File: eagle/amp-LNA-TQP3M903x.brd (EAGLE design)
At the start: 30 x 20 mm, 20 parts, among them J1 142-0701-851, J2 142-0701-851, U1 TQP3M903X

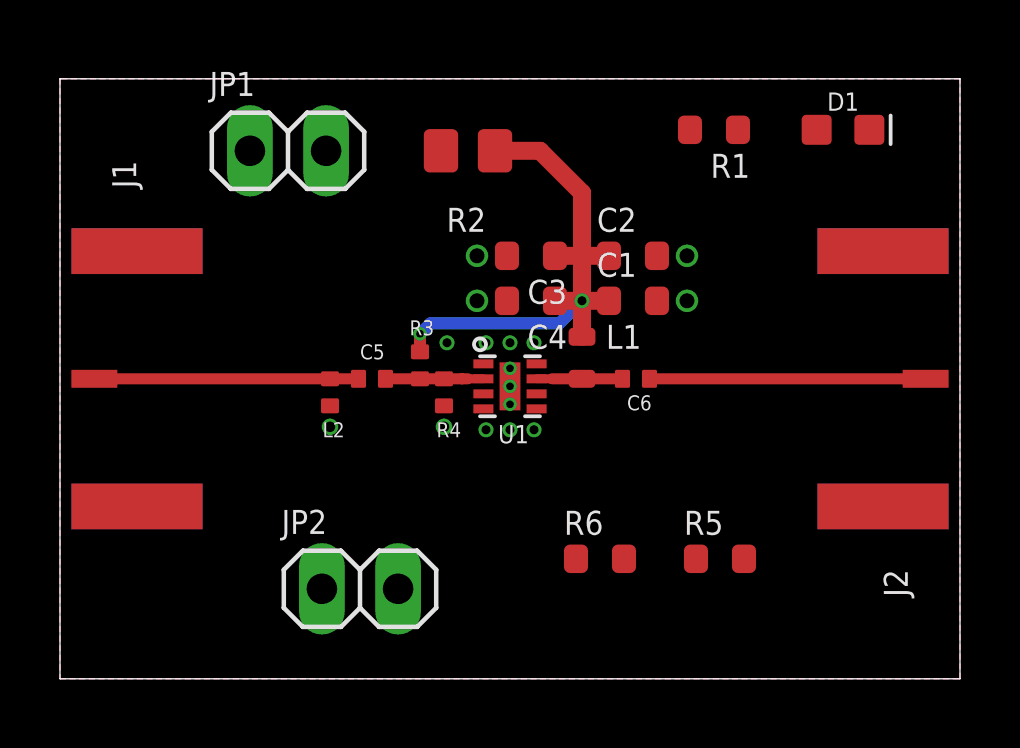
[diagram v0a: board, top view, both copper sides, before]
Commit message: Completed TQP3M903x layout
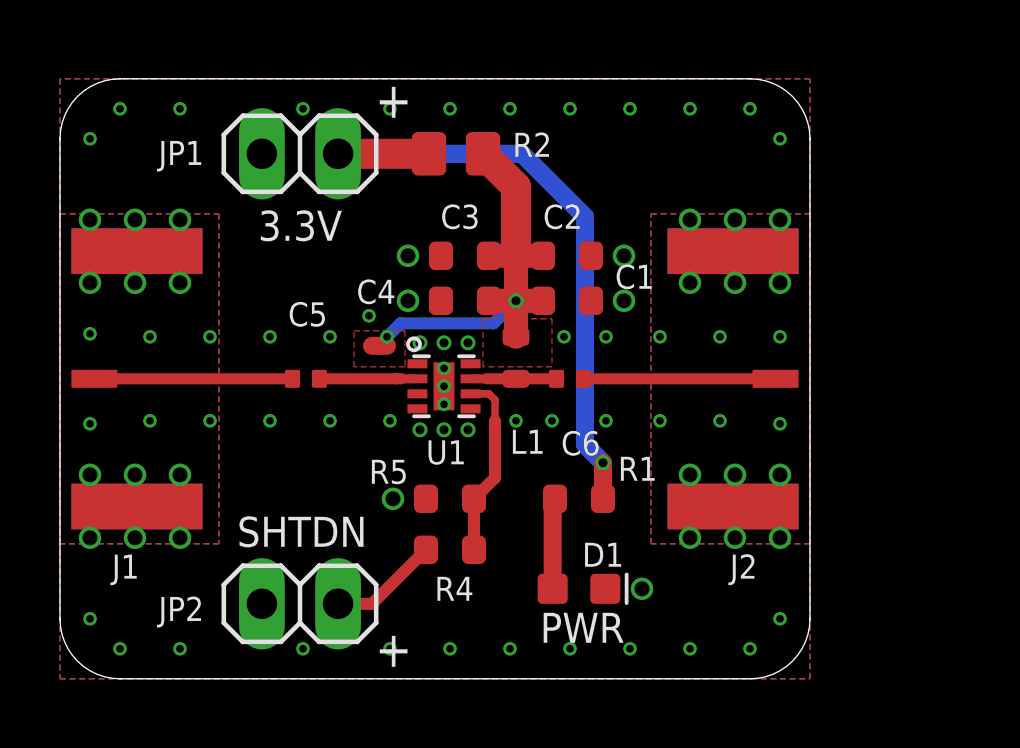
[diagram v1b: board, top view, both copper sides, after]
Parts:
- removed L2: ?, oresat-rcl:.0402-C-NOSILK
- removed R3: NP, oresat-rcl:.0402-C-NOSILK
- removed R6: 10k, oresat-rcl:.0603-B-NOSILK
- R4: value NP -> 33k; device oresat-rcl:.0402-C-NOSILK -> oresat-rcl:.0603-B-NOSILK
- R5: value 33k -> 10k
- moved D1 17.7 mm to (17.3, 3.00)
- moved R1 13.1 mm to (17.3, 6.00), turned to 0 degrees
- moved R5 9.22 mm to (13.0, 6.00)
- moved R4 5.25 mm to (13.0, 4.30), turned to 180 degrees
- moved J2 5.00 mm to (25.0, 10.0)
- moved C1 2.20 mm to (16.9, 12.6)
- moved C2 2.20 mm to (16.9, 14.1)
- moved C5 2.20 mm to (8.20, 10.0)
- moved C3 2.20 mm to (13.5, 14.1)
- moved C4 2.20 mm to (13.5, 12.6)
- moved C6 2.20 mm to (17.0, 10.0)
- moved L1 2.20 mm to (15.2, 10.7)
- moved U1 2.20 mm to (12.8, 9.75)
- moved JP2 2.06 mm to (8.00, 2.50)
- moved JP1 0.41 mm to (8.00, 17.5)
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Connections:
- net N$34 renamed RF_OUT
- removed net N$39: C5.1, J1.RF1, L2.1
- new net RF_IN: C5.1, J1.RF1
- net GND: now also R5.1; no longer L2.2, R4.1, R6.1
- net N$2: now also R4.1, R5.2; no longer R5.1, R6.2
- net N$3: now also R4.2; no longer R5.2
- net N$32: no longer R3.1, R4.2
- net N$47: no longer R3.2
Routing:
- net N$1: track 0.00 -> 21.8 mm, vias 0 -> 1
- net N$39: track 8.80 -> 0.00 mm
- net RF_IN: track 0.00 -> 6.60 mm
- net N$2: track 0.00 -> 6.19 mm
- net N$3: track 0.00 -> 3.68 mm
- net N$21: track 0.00 -> 3.03 mm
- net RF_OUT: track 9.20 -> 6.40 mm
- net N$47: track 18.3 -> 15.8 mm
- added copper zone on layer 15, net GND
- added copper zone on layer 2, net GND
- added copper zone on layer 1, net RF_IN
- added copper zone on layer 1, net RF_OUT
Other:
- board size 30 x 20 mm -> 25 x 20 mm
- board text added: "+"
- board text added: "3.3V"
- board text added: "LNA TQP3M903X PSAS / OreSat 2019-08-13 v1.0 V.M. KJ7AOG"
- board text added: "PWR"
- board text added: "SHTDN"

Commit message: Tune S band
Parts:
- added C7: 2.4p, oresat-rcl:.0402-C-NOSILK
- added L2: 2.7n, oresat-rcl:.0402-C-NOSILK
- C5, C6: value ? -> 100p
- L1: value ? -> 4.3n
- moved C5 3.20 mm to (5.00, 10.0)
- moved C6 3.00 mm to (20.0, 10.0)
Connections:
- net RF_IN renamed N$6
- removed net N$32: C5.2, U1.2
- new net N$4: C7.2, U1.2
- new net N$5: C5.2, C7.1, L2.1
- net GND: now also L2.2
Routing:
- net N$32: track 3.26 -> 0.00 mm
- net N$6: track 6.60 -> 3.40 mm
- net RF_OUT: track 6.40 -> 3.40 mm
- net N$28: track 2.87 -> 5.87 mm
- net N$5: track 0.00 -> 2.80 mm
- net N$4: track 0.00 -> 2.76 mm
- added copper zone on layer 1, net RF_IN
- removed copper zone on layer 1, net N$6
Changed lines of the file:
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@@
 <drawing>
 <settings>
-<setting alwaysvectorfont="no"/>
+<setting alwaysvectorfont="yes"/>
 <setting verticaltext="up"/>
 </settings>
@@
 <wire x1="2" y1="20" x2="0" y2="18" width="0" layer="20" curve="90"/>
 <polygon width="0.3" layer="29">
-<vertex x="0" y="4.5"/>
-<vertex x="0" y="15.5"/>
-<vertex x="5.3" y="15.5"/>
-<vertex x="5.3" y="11.5"/>
-<vertex x="11.4" y="11.5"/>
+<vertex x="0" y="8.9"/>
+<vertex x="0" y="11.1"/>
+<vertex x="11.4" y="11.1"/>
 <vertex x="11.4" y="10.6"/>
 <vertex x="14.2" y="10.6"/>
-<vertex x="14.2" y="11.5"/>
-<vertex x="19.7" y="11.5"/>
-<vertex x="19.7" y="15.5"/>
-<vertex x="25" y="15.5"/>
-<vertex x="25" y="4.5"/>
-<vertex x="19.7" y="4.5"/>
-<vertex x="19.7" y="8.5"/>
-<vertex x="14.2" y="8.5"/>
-<vertex x="14.2" y="8.9"/>
-<vertex x="11.4" y="8.9"/>
-<vertex x="11.4" y="8.5"/>
-<vertex x="5.3" y="8.5"/>
-<vertex x="5.3" y="4.5"/>
+<vertex x="14.2" y="11.1"/>
+<vertex x="25" y="11.1"/>
+<vertex x="25" y="8.9"/>
 </polygon>
 <text x="10.5" y="0.4" size="1.2" layer="21" font="vector" ratio="15">+</text>
@@
 </class>
 <class number="1" name="RF1" width="0" drill="0">
-<clearance class="1" value="0.4"/>
+<clearance class="1" value="0.5"/>
 </class>
 <class number="2" name="RF2" width="0" drill="0">
-<clearance class="2" value="0.6"/>
+<clearance class="2" value="0.4"/>
 </class>
 </classes>
@@
 <attribute name="NAME" x="13.5" y="12.6" size="0.3" layer="33" ratio="15" rot="R180" align="center"/>
 </element>
-<element name="C5" library="oresat-rcl" package=".0402-C-NOSILK" value="?" x="8.2" y="10" smashed="yes">
-<attribute name="NAME" x="7.6" y="11.75" size="0.8" layer="25" font="vector" ratio="15"/>
-<attribute name="NAME" x="8.2" y="10" size="0.2" layer="33" ratio="15" align="center"/>
-</element>
-<element name="C6" library="oresat-rcl" package=".0402-C-NOSILK" value="?" x="17" y="10" smashed="yes">
-<attribute name="NAME" x="16.7" y="7.45" size="0.8" layer="25" font="vector" ratio="15"/>
-<attribute name="NAME" x="17" y="10" size="0.2" layer="33" ratio="15" align="center"/>
+<element name="C5" library="oresat-rcl" package=".0402-C-NOSILK" value="100p" x="5" y="10" smashed="yes">
+<attribute name="NAME" x="4.5" y="11.55" size="0.8" layer="25" font="vector" ratio="15"/>
+<attribute name="NAME" x="5" y="10" size="0.2" layer="33" ratio="15" align="center"/>
+</element>
+<element name="C6" library="oresat-rcl" package=".0402-C-NOSILK" value="100p" x="20" y="10" smashed="yes">
+<attribute name="NAME" x="19.5" y="11.55" size="0.8" layer="25" font="vector" ratio="15"/>
+<attribute name="NAME" x="20" y="10" size="0.2" layer="33" ratio="15" align="center"/>
 </element>
 <element name="D1" library="SparkFun-LED" library_urn="urn:adsk.eagle:library:529" package="LED-0603" package3d_urn="urn:adsk.eagle:package:39354/1" value="GREEN" x="17.3" y="3" smashed="yes">
@@
 <attribute name="VALUE" x="5.46" y="-0.675" size="1.27" layer="27"/>
 </element>
-<element name="L1" library="oresat-rcl" package=".0603-C-NOSILK" value="?" x="15.2" y="10.7" smashed="yes" rot="R270">
+<element name="L1" library="oresat-rcl" package=".0603-C-NOSILK" value="4.3n" x="15.2" y="10.7" smashed="yes" rot="R270">
 <attribute name="NAME" x="15" y="7.5" size="0.8" layer="25" font="vector" ratio="15"/>
 <attribute name="NAME" x="15.2" y="10.7" size="0.3" layer="33" ratio="15" rot="R270" align="center"/>
@@
 <element name="U1" library="U-Qorvo-TQP3M903x-LNA" package="DFN8-2X2-WITH-PAD" value="TQP3M903X" x="12.8" y="9.75" smashed="yes" rot="R270">
 <attribute name="NAME" x="12.2" y="7.15" size="0.8" layer="25" font="vector" ratio="15"/>
+</element>
+<element name="C7" library="oresat-rcl" package=".0402-C-NOSILK" value="2.4p" x="8.7" y="10" smashed="yes">
+<attribute name="NAME" x="8.4" y="11.55" size="0.8" layer="25" font="vector" ratio="15"/>
+<attribute name="NAME" x="8.7" y="10" size="0.2" layer="33" ratio="15" align="center"/>
+</element>
+<element name="L2" library="oresat-rcl" package=".0402-C-NOSILK" value="2.7n" x="7.55" y="9.55" smashed="yes" rot="R270">
+<attribute name="NAME" x="7.15" y="7.8" size="0.8" layer="25" font="vector" ratio="15"/>
+<attribute name="NAME" x="7.55" y="9.55" size="0.3" layer="33" ratio="15" rot="R270" align="center"/>
 </element>
 </elements>
@@
 </polygon>
 <polygon width="0.2" layer="1" pour="cutout">
-<vertex x="9.8" y="11.6"/>
+<vertex x="10.2" y="11.6"/>
 <vertex x="11.5" y="11.6"/>
 <vertex x="11.5" y="10.4"/>
-<vertex x="9.8" y="10.4"/>
+<vertex x="10.2" y="10.4"/>
 </polygon>
 <polygon width="0.3" layer="1" thermals="no">
@@
 <via x="3" y="8.6" extent="1-16" drill="0.254"/>
 <via x="5" y="8.6" extent="1-16" drill="0.254"/>
-<via x="7" y="8.6" extent="1-16" drill="0.254"/>
+<via x="6.7" y="8.6" extent="1-16" drill="0.254"/>
 <via x="9" y="8.6" extent="1-16" drill="0.254"/>
 <via x="11" y="8.6" extent="1-16" drill="0.254"/>
@@
 <via x="11.1" y="6" extent="1-16" drill="0.5"/>
 <via x="19.4" y="3" extent="1-16" drill="0.5"/>
+<contactref element="L2" pad="2"/>
+<polygon width="0.3" layer="1" thermals="no">
+<vertex x="6.9" y="9.1"/>
+<vertex x="8.3" y="9.1"/>
+<vertex x="8.3" y="8.4"/>
+<vertex x="6.9" y="8.4"/>
+</polygon>
 </signal>
 <signal name="N$28" class="1">
@@
 <contactref element="C6" pad="1"/>
 <contactref element="L1" pad="2"/>
+<wire x1="19.55" y1="10" x2="15.2" y2="10" width="0.37" layer="1"/>
+<wire x1="15.2" y1="10" x2="14.2" y2="10" width="0.37" layer="1"/>
 <wire x1="14.2" y1="10" x2="13.685" y2="10" width="0.3" layer="1"/>
-<wire x1="16.55" y1="10" x2="14.2" y2="10" width="0.37" layer="1"/>
-<wire x1="14.2" y1="10" x2="15.2" y2="10" width="0" layer="19" extent="1-1"/>
-</signal>
-<signal name="N$32" class="1">
-<contactref element="C5" pad="2"/>
-<contactref element="U1" pad="2"/>
-<wire x1="11.4" y1="10" x2="11.915" y2="10" width="0.3" layer="1"/>
-<wire x1="8.65" y1="10" x2="11.2" y2="10" width="0.37" layer="1"/>
-<wire x1="11.2" y1="10" x2="11.4" y2="10" width="0.37" layer="1"/>
-</signal>
-<signal name="RF_OUT" class="2">
+</signal>
+<signal name="RF_OUT" class="1">
 <contactref element="C6" pad="2"/>
 <contactref element="J2" pad="RF1"/>
-<wire x1="17.45" y1="10" x2="23.854" y2="10" width="0.37" layer="1"/>
+<wire x1="20.45" y1="10" x2="23.854" y2="10" width="0.37" layer="1"/>
 <polygon width="0.2" layer="1">
 <vertex x="23.2" y="10.2"/>
@@
 </signal>
 <signal name="RF_IN" class="2">
-<contactref element="C5" pad="1"/>
-<contactref element="J1" pad="RF1"/>
-<wire x1="7.75" y1="10" x2="1.146" y2="10" width="0.37" layer="1"/>
 <polygon width="0.2" layer="1">
 <vertex x="1.7" y="10.2"/>
@@
 <wire x1="16.1" y1="12.6" x2="15.2" y2="12.6" width="0.8" layer="1"/>
 <wire x1="14.3" y1="12.6" x2="15.2" y2="12.6" width="0.8" layer="1"/>
-<via x="10.9" y="11.4" extent="1-16" drill="0.254"/>
-<wire x1="10.9" y1="11.4" x2="11.35" y2="11.85" width="0.4" layer="16"/>
+<via x="11" y="11.4" extent="1-16" drill="0.254"/>
+<wire x1="11" y1="11.4" x2="11.45" y2="11.85" width="0.4" layer="16"/>
 <wire x1="14.45" y1="11.85" x2="15.2" y2="12.6" width="0.4" layer="16"/>
 <via x="15.2" y="12.6" extent="1-16" drill="0.3"/>
-<wire x1="11.35" y1="11.85" x2="14.45" y2="11.85" width="0.4" layer="16"/>
+<wire x1="11.45" y1="11.85" x2="14.45" y2="11.85" width="0.4" layer="16"/>
 <wire x1="14.1" y1="17.5" x2="15.2" y2="16.4" width="1" layer="1"/>
 <wire x1="15.2" y1="16.4" x2="15.2" y2="14.1" width="1" layer="1"/>
-<wire x1="10.9" y1="11.4" x2="10.9" y2="11.1" width="0.4" layer="1"/>
-<wire x1="10.9" y1="11.1" x2="10.4" y2="11.1" width="0.6" layer="1"/>
+<wire x1="11" y1="11.4" x2="11" y2="11.1" width="0.4" layer="1"/>
+<wire x1="11" y1="11.1" x2="10.8" y2="11.1" width="0.6" layer="1"/>
 </signal>
 <signal name="N$2">
@@
 <wire x1="10.4" y1="2.5" x2="12.2" y2="4.3" width="0.4" layer="1"/>
 </signal>
+<signal name="N$4" class="1">
+<contactref element="C7" pad="2"/>
+<contactref element="U1" pad="2"/>
+<wire x1="11.4" y1="10" x2="9.15" y2="10" width="0.37" layer="1"/>
+<wire x1="11.915" y1="10" x2="11.4" y2="10" width="0.3" layer="1"/>
+</signal>
+<signal name="N$5" class="1">
+<contactref element="C7" pad="1"/>
+<contactref element="C5" pad="2"/>
+<contactref element="L2" pad="1"/>
+<wire x1="8.25" y1="10" x2="5.45" y2="10" width="0.37" layer="1"/>
+<wire x1="8.25" y1="10" x2="7.55" y2="10" width="0" layer="19" extent="1-1"/>
+</signal>
+<signal name="N$6" class="1">
+<contactref element="C5" pad="1"/>
+<contactref element="J1" pad="RF1"/>
+<wire x1="4.55" y1="10" x2="1.146" y2="10" width="0.37" layer="1"/>
+</signal>
 </signals>

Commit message: Minor fixes
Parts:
- removed C7: 2.4p, oresat-rcl:.0402-C-NOSILK
- C5: value 100p -> 2.4p
- moved C5 3.70 mm to (8.70, 10.0)
- moved C6 2.00 mm to (18.0, 10.0)
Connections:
- removed net N$5: C5.2, C7.1, L2.1
- removed net N$6: C5.1, J1.RF1
- new net RF_IN: C5.1, J1.RF1, L2.1
- net N$4: now also C5.2; no longer C7.2
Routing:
- net RF_IN: track 0.00 -> 7.10 mm
- net N$6: track 3.40 -> 0.00 mm
- net N$5: track 2.80 -> 0.00 mm
- net RF_OUT: track 3.40 -> 5.40 mm
- net N$28: track 5.87 -> 3.87 mm
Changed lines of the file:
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@@
 <drawing>
 <settings>
-<setting alwaysvectorfont="yes"/>
+<setting alwaysvectorfont="no"/>
 <setting verticaltext="up"/>
 </settings>
@@
 <vertex x="25" y="8.9"/>
 </polygon>
-<text x="10.5" y="0.4" size="1.2" layer="21" font="vector" ratio="15">+</text>
-<text x="10.5" y="18.7" size="1.2" layer="21" font="vector" ratio="15">+</text>
+<text x="10.2" y="0.4" size="1.2" layer="21" font="vector" ratio="15">+</text>
+<text x="10.2" y="18.7" size="1.2" layer="21" font="vector" ratio="15">+</text>
 <text x="6.6" y="14.6" size="1" layer="21" font="vector" ratio="15">3.3V</text>
 <text x="5.9" y="4.4" size="1" layer="21" font="vector" ratio="15">SHTDN</text>
@@
 </class>
 <class number="2" name="RF2" width="0" drill="0">
-<clearance class="2" value="0.4"/>
+<clearance class="2" value="0.8"/>
 </class>
 </classes>
@@
 <attribute name="NAME" x="13.5" y="12.6" size="0.3" layer="33" ratio="15" rot="R180" align="center"/>
 </element>
-<element name="C5" library="oresat-rcl" package=".0402-C-NOSILK" value="100p" x="5" y="10" smashed="yes">
-<attribute name="NAME" x="4.5" y="11.55" size="0.8" layer="25" font="vector" ratio="15"/>
-<attribute name="NAME" x="5" y="10" size="0.2" layer="33" ratio="15" align="center"/>
-</element>
-<element name="C6" library="oresat-rcl" package=".0402-C-NOSILK" value="100p" x="20" y="10" smashed="yes">
-<attribute name="NAME" x="19.5" y="11.55" size="0.8" layer="25" font="vector" ratio="15"/>
-<attribute name="NAME" x="20" y="10" size="0.2" layer="33" ratio="15" align="center"/>
+<element name="C6" library="oresat-rcl" package=".0402-C-NOSILK" value="100p" x="18" y="10" smashed="yes">
+<attribute name="NAME" x="17.5" y="11.55" size="0.8" layer="25" font="vector" ratio="15"/>
+<attribute name="NAME" x="18" y="10" size="0.2" layer="33" ratio="15" align="center"/>
 </element>
 <element name="D1" library="SparkFun-LED" library_urn="urn:adsk.eagle:library:529" package="LED-0603" package3d_urn="urn:adsk.eagle:package:39354/1" value="GREEN" x="17.3" y="3" smashed="yes">
@@
 <attribute name="NAME" x="12.2" y="7.15" size="0.8" layer="25" font="vector" ratio="15"/>
 </element>
-<element name="C7" library="oresat-rcl" package=".0402-C-NOSILK" value="2.4p" x="8.7" y="10" smashed="yes">
+<element name="C5" library="oresat-rcl" package=".0402-C-NOSILK" value="2.4p" x="8.7" y="10" smashed="yes">
 <attribute name="NAME" x="8.4" y="11.55" size="0.8" layer="25" font="vector" ratio="15"/>
 <attribute name="NAME" x="8.7" y="10" size="0.2" layer="33" ratio="15" align="center"/>
@@
 <via x="3" y="8.6" extent="1-16" drill="0.254"/>
 <via x="5" y="8.6" extent="1-16" drill="0.254"/>
-<via x="6.7" y="8.6" extent="1-16" drill="0.254"/>
+<via x="7" y="8.6" extent="1-16" drill="0.254"/>
 <via x="9" y="8.6" extent="1-16" drill="0.254"/>
 <via x="11" y="8.6" extent="1-16" drill="0.254"/>
@@
 <via x="15" y="1" extent="1-16" drill="0.254"/>
 <via x="13" y="1" extent="1-16" drill="0.254"/>
-<via x="11" y="1" extent="1-16" drill="0.254"/>
+<via x="11.2" y="1" extent="1-16" drill="0.254"/>
 <via x="1" y="18" extent="1-16" drill="0.254"/>
 <via x="2" y="19" extent="1-16" drill="0.254"/>
@@
 <via x="15" y="19" extent="1-16" drill="0.254"/>
 <via x="13" y="19" extent="1-16" drill="0.254"/>
-<via x="11" y="19" extent="1-16" drill="0.254"/>
+<via x="11.2" y="19" extent="1-16" drill="0.254"/>
 <via x="11.1" y="6" extent="1-16" drill="0.5"/>
 <via x="19.4" y="3" extent="1-16" drill="0.5"/>
@@
 <vertex x="6.9" y="8.4"/>
 </polygon>
+<via x="7.6" y="8.6" extent="1-16" drill="0.254"/>
+<wire x1="7.6" y1="8.6" x2="7.55" y2="9.1" width="0" layer="19" extent="1-1"/>
 </signal>
 <signal name="N$28" class="1">
@@
 <contactref element="C6" pad="1"/>
 <contactref element="L1" pad="2"/>
-<wire x1="19.55" y1="10" x2="15.2" y2="10" width="0.37" layer="1"/>
+<wire x1="17.55" y1="10" x2="15.2" y2="10" width="0.37" layer="1"/>
 <wire x1="15.2" y1="10" x2="14.2" y2="10" width="0.37" layer="1"/>
 <wire x1="14.2" y1="10" x2="13.685" y2="10" width="0.3" layer="1"/>
 </signal>
-<signal name="RF_OUT" class="1">
+<signal name="RF_OUT" class="2">
 <contactref element="C6" pad="2"/>
 <contactref element="J2" pad="RF1"/>
-<wire x1="20.45" y1="10" x2="23.854" y2="10" width="0.37" layer="1"/>
+<wire x1="18.45" y1="10" x2="23.854" y2="10" width="0.37" layer="1"/>
 <polygon width="0.2" layer="1">
 <vertex x="23.2" y="10.2"/>
@@
 <vertex x="1.7" y="9.8"/>
 </polygon>
+<contactref element="C5" pad="1"/>
+<contactref element="L2" pad="1"/>
+<contactref element="J1" pad="RF1"/>
+<wire x1="8.25" y1="10" x2="7.55" y2="10" width="0.37" layer="1"/>
+<wire x1="7.55" y1="10" x2="1.146" y2="10" width="0.37" layer="1"/>
 </signal>
 <signal name="N$47">
@@
 </signal>
 <signal name="N$4" class="1">
-<contactref element="C7" pad="2"/>
+<contactref element="C5" pad="2"/>
 <contactref element="U1" pad="2"/>
 <wire x1="11.4" y1="10" x2="9.15" y2="10" width="0.37" layer="1"/>
 <wire x1="11.915" y1="10" x2="11.4" y2="10" width="0.3" layer="1"/>
-</signal>
-<signal name="N$5" class="1">
-<contactref element="C7" pad="1"/>
-<contactref element="C5" pad="2"/>
-<contactref element="L2" pad="1"/>
-<wire x1="8.25" y1="10" x2="5.45" y2="10" width="0.37" layer="1"/>
-<wire x1="8.25" y1="10" x2="7.55" y2="10" width="0" layer="19" extent="1-1"/>
-</signal>
-<signal name="N$6" class="1">
-<contactref element="C5" pad="1"/>
-<contactref element="J1" pad="RF1"/>
-<wire x1="4.55" y1="10" x2="1.146" y2="10" width="0.37" layer="1"/>
 </signal>
 </signals>
@@
 <mfgpreviewcolor name="substratecolor" color="0xFF786E46"/>
 </mfgpreviewcolors>
+<errors>
+</errors>
 </board>
 </drawing>
